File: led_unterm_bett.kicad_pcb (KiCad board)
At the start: 2 copper layers, 27 parts, among them J1 Conn_01x03, J2 Conn_01x03, J3 Conn_01x03, J4 Conn_01x02, J5 Screw_Terminal_01x02, J6 Conn_01x04, Q1 BSS138, Q2 BSS138, Q3 BSS138, U1 NodeMCU1.0(ESP-12E), U2 LM7805_TO220

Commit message: placement complete
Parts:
- C1, C2, C3, C4, C5, D1, D2, D3, Q1, Q2, Q3, R1, R2, R3, R4, R5: moved to B.Cu
- J1, J3: footprint Pin_Headers:Pin_Header_Straight_1x03_Pitch1.00mm_SMD_Pin1Left -> Pin_Headers:Pin_Header_Straight_1x03_Pitch2.54mm
- J2: footprint Pin_Headers:Pin_Header_Straight_1x03_Pitch1.00mm_SMD_Pin1Right -> Pin_Headers:Pin_Header_Straight_1x03_Pitch2.54mm
- J4: footprint Pin_Headers:Pin_Header_Straight_1x02_Pitch1.27mm_SMD_Pin1Right -> Pin_Headers:Pin_Header_Straight_1x02_Pitch2.54mm
- J6: footprint Pin_Headers:Pin_Header_Straight_1x04_Pitch2.54mm_SMD_Pin1Right -> Pin_Headers:Pin_Header_Straight_1x04_Pitch2.54mm
- moved J5 45.3 mm to (124.5, 66.6)
- moved J6 40.9 mm to (143.1, 64.5), turned to 270 degrees
- moved J3 40.9 mm to (153.9, 64.5), turned to 270 degrees
- moved J2 36.9 mm to (153.9, 68.5), turned to 270 degrees
- moved C6 33.5 mm to (129.0, 77.8), turned to 180 degrees
- moved J1 32.9 mm to (153.9, 72.5), turned to 270 degrees
- moved D3 31.7 mm to (166.1, 78.6), turned to 90 degrees
- moved D2 29.7 mm to (162.2, 78.6), turned to 90 degrees
- moved D1 28.2 mm to (158.5, 78.6), turned to 90 degrees
- moved J4 27.4 mm to (132.0, 126.9), turned to 270 degrees
- moved C5 24.9 mm to (162.8, 125.4), turned to 270 degrees
- moved C8 24.9 mm to (125.8, 115.2)
- moved C7 23.1 mm to (125.7, 101.1)
- moved R1 22.9 mm to (162.6, 87.0), turned to 270 degrees
- moved C3 22.0 mm to (140.2, 125.4), turned to 90 degrees
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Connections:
- J1 pad 1: GND -> Net-(D1-Pad2)
- J1 pad 2: Net-(D1-Pad2) -> +5V
- J1 pad 3: +5V -> GND
- J2 pad 1: GND -> Net-(D2-Pad2)
- J2 pad 2: Net-(D2-Pad2) -> +5V
- J2 pad 3: +5V -> GND
- J3 pad 1: GND -> Net-(D3-Pad2)
- J3 pad 2: Net-(D3-Pad2) -> +5V
- J3 pad 3: +5V -> GND
- J6 pad 1: +12V -> Net-(J6-Pad1)
- J6 pad 4: Net-(J6-Pad4) -> +12V
- Q1 pad 3: Net-(J6-Pad2) -> Net-(J6-Pad1)
- Q2 pad 3: Net-(J6-Pad3) -> Net-(J6-Pad2)
- Q3 pad 3: Net-(J6-Pad4) -> Net-(J6-Pad3)
- U1 pad 1: Net-(U1-Pad1) -> (no net)
- U1 pad 13: Net-(U1-Pad13) -> (no net)
- U1 pad 18: Net-(U1-Pad18) -> (no net)
- U1 pad 19: Net-(U1-Pad19) -> (no net)
- U1 pad 2: Net-(U1-Pad2) -> (no net)
- U1 pad 20: Net-(U1-Pad20) -> (no net)
- U1 pad 21: Net-(U1-Pad21) -> (no net)
- U1 pad 27: Net-(U1-Pad27) -> (no net)
- U1 pad 28: Net-(U1-Pad28) -> (no net)
- U1 pad 29: Net-(U1-Pad29) -> (no net)
- U1 pad 3: Net-(U1-Pad3) -> (no net)
- U1 pad 4: Net-(U1-Pad4) -> (no net)
- U1 pad 5: Net-(U1-Pad5) -> (no net)
- U1 pad 6: Net-(U1-Pad6) -> (no net)
- U1 pad 7: Net-(U1-Pad7) -> (no net)
- U1 pad 8: Net-(U1-Pad8) -> (no net)
- U1 pad 9: Net-(U1-Pad9) -> (no net)
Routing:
- added copper zone on B.Cu, net GND
- added copper zone on F.Cu, net GND
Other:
- board outline added: 68.7 x 94.9 mm

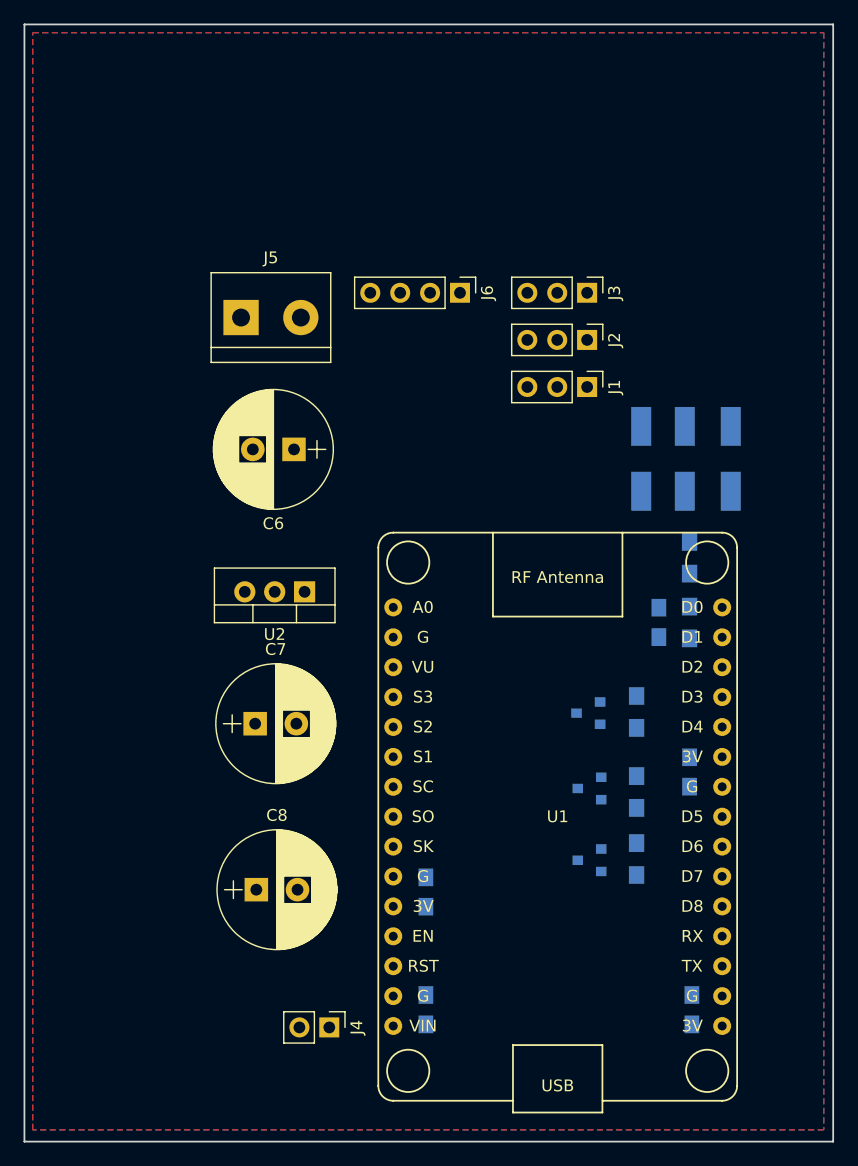
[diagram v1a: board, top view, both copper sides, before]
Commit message: finish routing for etched PCB
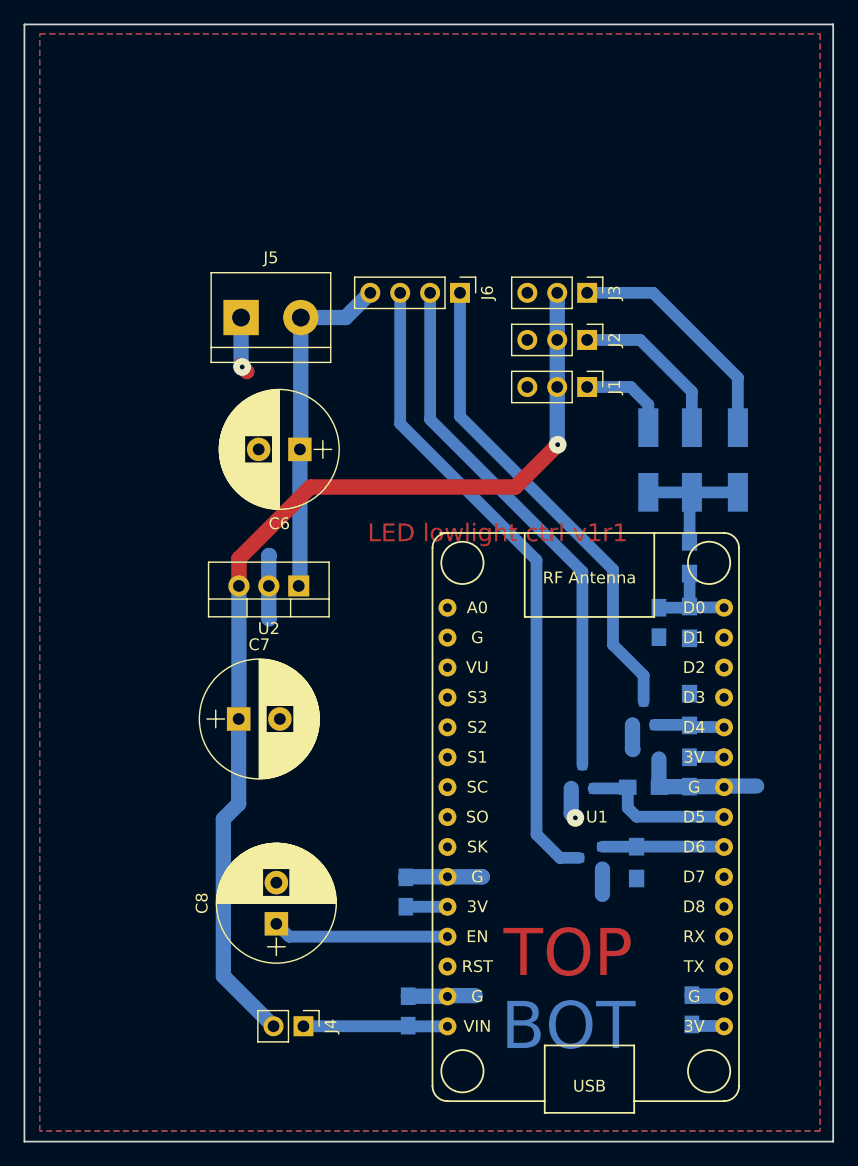
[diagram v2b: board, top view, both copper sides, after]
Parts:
- U1: footprint ESP8266:NodeMCU1.0(12-E) -> ESP8266:ESP12F-Devkit-V3
- moved Q1 4.70 mm to (158.7, 100.2), turned to 90 degrees
- moved R3 4.50 mm to (162.6, 99.9), turned to 90 degrees
- moved C8 3.36 mm to (127.5, 118.1), turned to 90 degrees
- moved U1 3.00 mm to (154.1, 110.3)
- moved J4 2.20 mm to (129.8, 126.8)
- moved C2 1.70 mm to (138.5, 115.4)
- moved C3 1.50 mm to (138.7, 125.5)
- moved C7 1.46 mm to (124.3, 100.7)
- moved Q2 1.17 mm to (153.5, 105.6), turned to 90 degrees
- moved R4 0.72 mm to (158.7, 106.5), turned to 0 degrees
- moved U2 0.71 mm to (129.4, 89.4)
- moved D2 0.61 mm to (162.8, 78.7)
- moved D1 0.61 mm to (159.1, 78.7)
- moved D3 0.61 mm to (166.7, 78.7)
- moved C6 0.50 mm to (129.5, 77.8)
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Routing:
- net +5V: track 0.00 -> 86.0 mm, vias 0 -> 1
- net Net-(J6-Pad3): track 0.00 -> 55.2 mm
- net Net-(J6-Pad2): track 0.00 -> 45.5 mm
- net GND: track 0.00 -> 43.0 mm, vias 0 -> 2
- net Net-(J6-Pad1): track 0.00 -> 41.2 mm
- net +12V: track 0.00 -> 29.6 mm
- net Net-(D3-Pad2): track 0.00 -> 20.0 mm
- net Net-(C8-Pad1): track 0.00 -> 15.0 mm
- net Net-(D2-Pad2): track 0.00 -> 13.8 mm
- net Net-(Q2-Pad1): track 0.00 -> 13.0 mm
- net Net-(C3-Pad1): track 0.00 -> 12.2 mm
- net Net-(D1-Pad1): track 0.00 -> 11.9 mm
- net Net-(Q3-Pad1): track 0.00 -> 10.2 mm
- net Net-(C1-Pad2): track 0.00 -> 8.18 mm
- net Net-(D1-Pad2): track 0.00 -> 7.77 mm
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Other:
- net class Default: clearance 0.2 -> 0.25; trace_width 0.25 -> 1; via_dia 0.6 -> 1.5
- net class Power added: clearance 0.3, trace_width 1.3, via_dia 1.5, via_drill 0.4
- rule trace_clearance: 0.2 -> 0.25
- board text added: "BOT"
- board text added: "LED lowlight ctrl v1r1"
- board text added: "TOP"

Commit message: kicad 4->5, jlcpcb drc
Load design rules from https://github.com/sethhillbrand/kicad_templates.
Used rules for jlcpcb.com
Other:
- rule pad_to_mask_clearance: 0.2 -> 0
- rule trace_min: 0.2 -> 0.127
- rule via_min_size: 0.4 -> 0.6

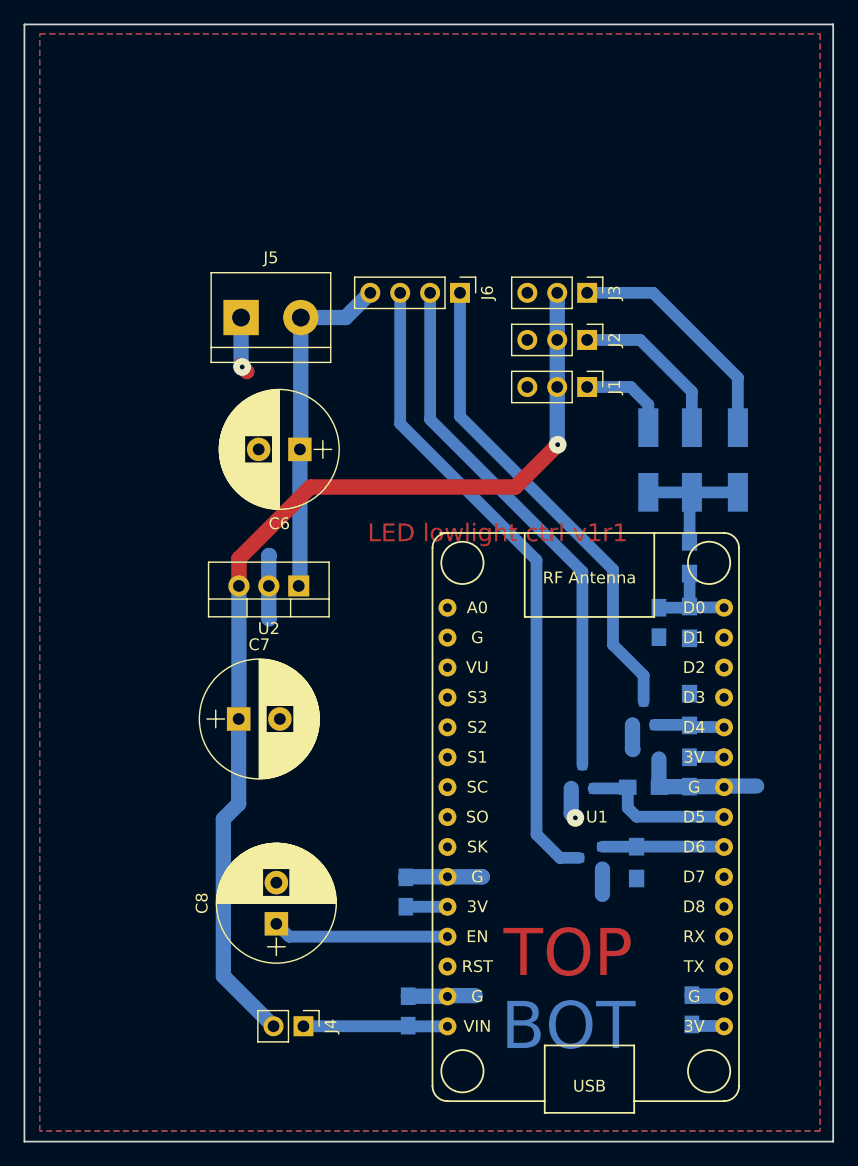
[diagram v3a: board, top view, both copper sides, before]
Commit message: shrink board and add mounting holes
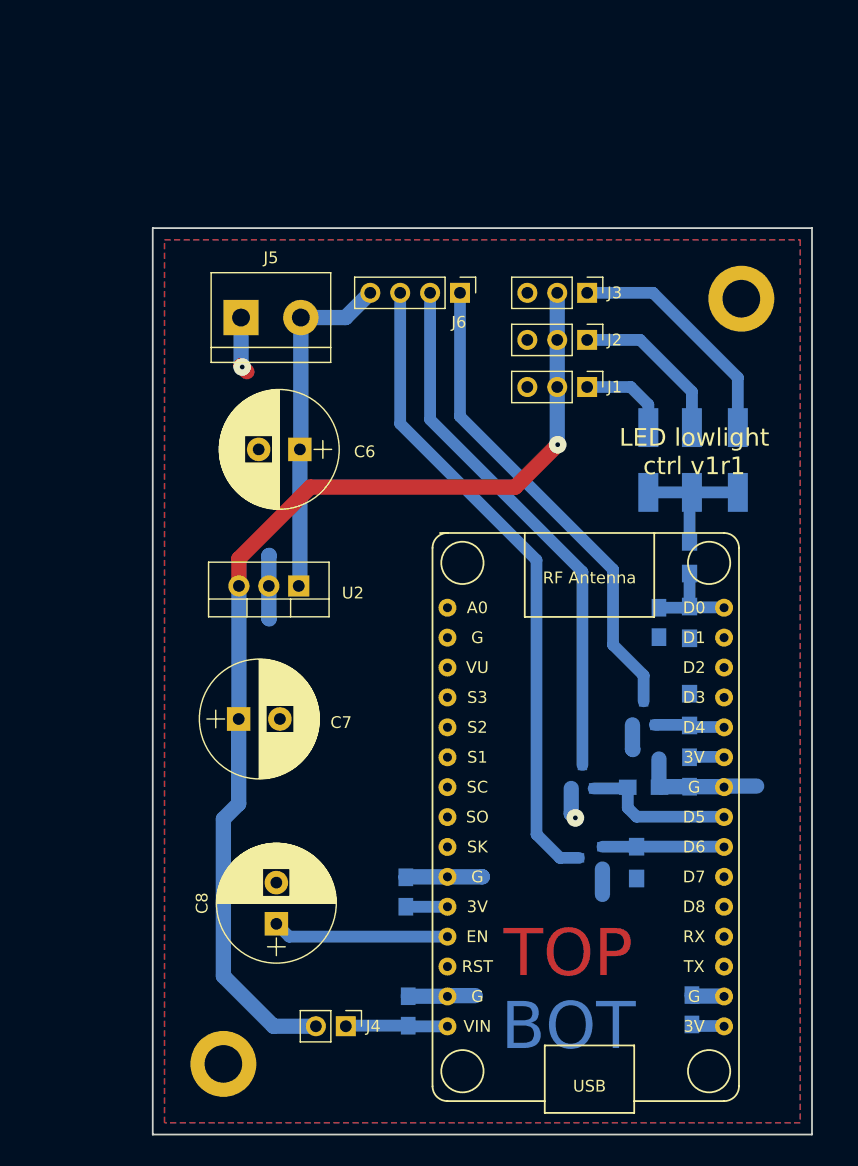
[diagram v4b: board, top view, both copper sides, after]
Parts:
- added REF**: MountingHole_3.2mm_M3_DIN965_Pad, Mounting_Holes:MountingHole_3.2mm_M3_DIN965_Pad, F.Cu at (123.0, 130.0)
- added REF**: MountingHole_3.2mm_M3_DIN965_Pad, Mounting_Holes:MountingHole_3.2mm_M3_DIN965_Pad, F.Cu at (167.0, 65.0)
- moved J4 3.60 mm to (133.4, 126.8)
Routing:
- net +5V: track 86.0 -> 89.6 mm
- net Net-(C3-Pad1): track 12.2 -> 8.71 mm
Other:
- board size 68.7 x 94.9 mm -> 56 x 77 mm

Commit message: migrate to kicad 6.0
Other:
- net class Default removed
- net class Power removed

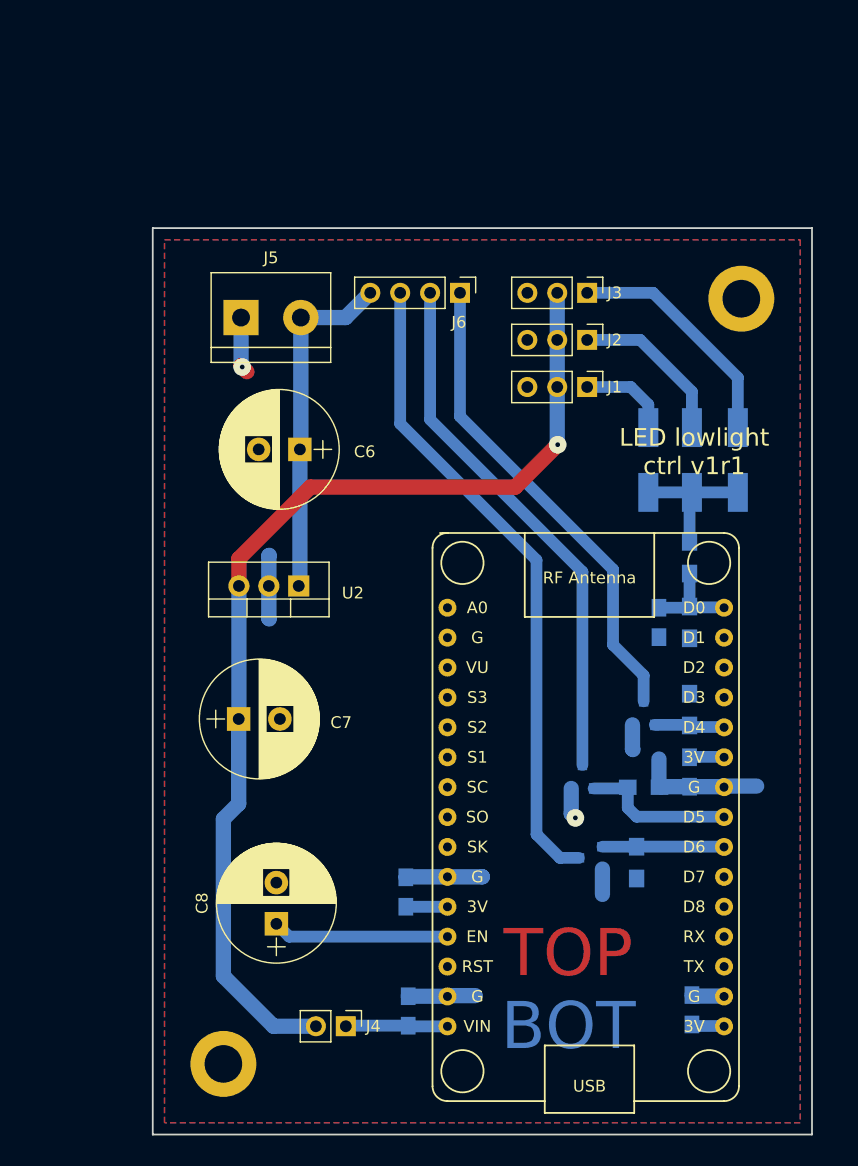
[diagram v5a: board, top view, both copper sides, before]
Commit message: update some resistor values
so the 0805er E-series set lasts longer ;-)
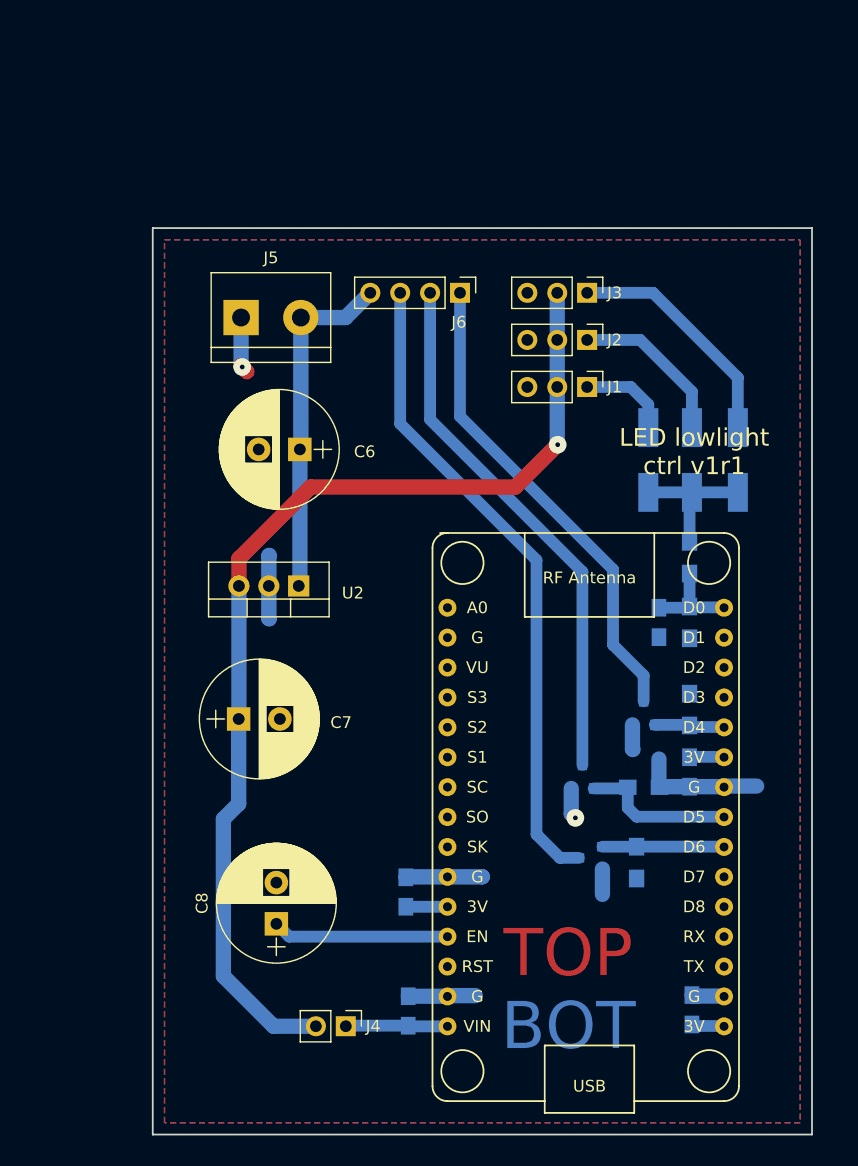
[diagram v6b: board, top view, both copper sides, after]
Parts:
- removed REF** (x2): MountingHole_3.2mm_M3_DIN965_Pad, Mounting_Holes:MountingHole_3.2mm_M3_DIN965_Pad
- R1: value 11k -> 12k
- R3, R4, R5: value 100k -> 91k
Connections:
- U1 pad 1: (no net) -> unconnected-(U1-Pad1)
- U1 pad 13: (no net) -> unconnected-(U1-Pad13)
- U1 pad 18: (no net) -> unconnected-(U1-Pad18)
- U1 pad 19: (no net) -> unconnected-(U1-Pad19)
- U1 pad 2: (no net) -> unconnected-(U1-Pad2)
- U1 pad 20: (no net) -> unconnected-(U1-Pad20)
- U1 pad 21: (no net) -> unconnected-(U1-Pad21)
- U1 pad 27: (no net) -> unconnected-(U1-Pad27)
- U1 pad 28: (no net) -> unconnected-(U1-Pad28)
- U1 pad 29: (no net) -> unconnected-(U1-Pad29)
- U1 pad 3: (no net) -> unconnected-(U1-Pad3)
- U1 pad 4: (no net) -> unconnected-(U1-Pad4)
- U1 pad 5: (no net) -> unconnected-(U1-Pad5)
- U1 pad 6: (no net) -> unconnected-(U1-Pad6)
- U1 pad 7: (no net) -> unconnected-(U1-Pad7)
- U1 pad 8: (no net) -> unconnected-(U1-Pad8)
- U1 pad 9: (no net) -> unconnected-(U1-Pad9)
